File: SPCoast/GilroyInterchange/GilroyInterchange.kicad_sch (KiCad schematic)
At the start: 31 parts, among them SW777 777, SW781 781

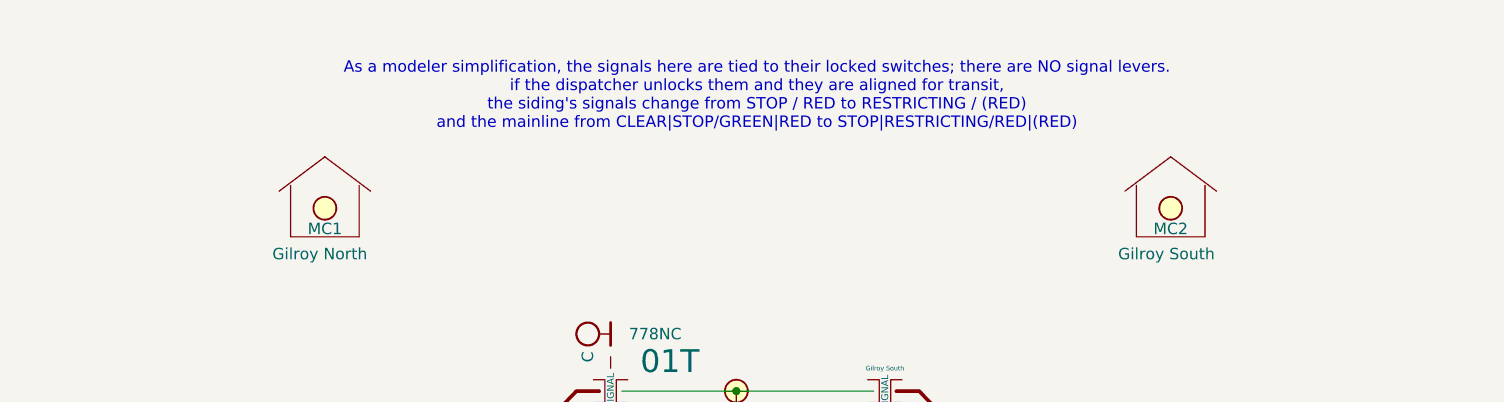
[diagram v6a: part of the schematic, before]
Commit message: SPCoast: owner's edits: Interlocking symbol on every Trackplan; MAIN HOUSE is STRUCTURE/CONTROL_POINT (baseline)
Each plant has one Interlocking symbol (Value is the authoritative name) and
every MAIN HOUSE's Interlocking pin is wired to it. Library Role/Kind:
Interlocking is STRUCTURE/INTERLOCKING, MAIN HOUSE is STRUCTURE/CONTROL_POINT
(refreshed on all instances by the owner).

Verified: one Interlocking symbol per plant; every house shares a net with it;
net counts are one higher than before in each plant (Christopher 34, Corporal
27, GilroyCalTrain 28, GilroyInterchange 23, Luchessa 35, Sargent 19,
Watsonville 97); no root-UUID regression; no symbol moved or removed.

Co-Authored-By: Claude Sonnet 5.5 <noreply@anthropic.com>
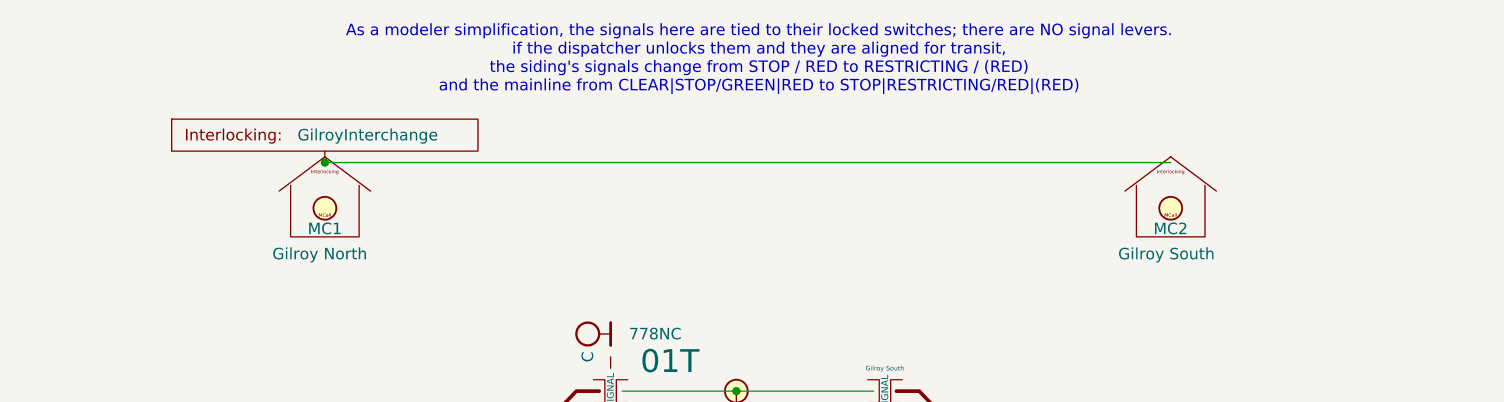
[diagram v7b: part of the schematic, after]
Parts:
- added Plant1: ${TITLE}, symbol Railroad:Interlocking
- HOUSE1, HOUSE2: Kind (none) -> CONTROL_POINT; Role CONTROL_POINT -> STRUCTURE
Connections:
- new net: HOUSE1.2 (Interlocking), HOUSE2.2 (Interlocking), Plant1.1 (Interlocking)
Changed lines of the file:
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@@
 	(text "As a modeler simplification, the signals here are tied to their locked switches; there are NO signal levers.\nif the dispatcher unlocks them and they are aligned for transit, \nthe siding's signals change from STOP / RED to RESTRICTING / (RED)\nand the mainline from CLEAR|STOP/GREEN|RED to STOP|RESTRICTING/RED|(RED)"
 		(exclude_from_sim no)
-		(at 122.936 28.194 0)
+		(at 123.19 24.13 0)
 		(effects
 			(font
@@
 	)
 	(junction
+		(at 74.93 35.56)
+		(diameter 0)
+		(color 0 0 0 0)
+	)
+	(junction
 		(at 63.5 77.47)
 		(diameter 0)
@@
 		(stroke
 			(width 0.4064)
+			(type default)
+		)
+	)
+	(wire
+		(pts
+			(xy 74.93 35.56) (xy 168.91 35.56)
+		)
+		(stroke
+			(width 0)
 			(type default)
 		)
@@
 			)
 		)
-		(property "Description" "Rrepresents the Control Point Maintainer Bungalow (plus optional Maintainer Call)"
+		(property "Description" "The Control Point Maintainer Bungalow (plus optional Maintainer Call)"
 			(at 168.91 46.355 0)
 			(hide yes)
@@
 		)
 		(property "Milepost" "78.1"
-			(at 168.91 46.36 0)
-			(hide yes)
-			(show_name no)
-			(do_not_autoplace no)
-			(effects
-				(font
-					(size 1.27 1.27)
-				)
-			)
-		)
-		(property "Role" "CONTROL_POINT"
-			(at 168.91 40.64 0)
+			(at 168.91 46.355 0)
+			(hide yes)
+			(show_name no)
+			(do_not_autoplace no)
+			(effects
+				(font
+					(size 1.27 1.27)
+				)
+			)
+		)
+		(property "Role" "STRUCTURE"
+			(at 153.67 38.1 0)
+			(hide yes)
+			(show_name no)
+			(do_not_autoplace no)
+			(effects
+				(font
+					(size 1.27 1.27)
+				)
+			)
+		)
+		(property "Kind" "CONTROL_POINT"
+			(at 155.575 40.132 0)
 			(hide yes)
 			(show_name no)
@@
 		)
 		(pin "1"
+		)
+		(pin "2"
 		)
 		(instances
@@
 	)
 	(symbol
+		(lib_id "Railroad:Interlocking")
+		(at 74.93 35.56 0)
+		(unit 1)
+		(body_style 1)
+		(exclude_from_sim no)
+		(in_bom yes)
+		(on_board yes)
+		(in_pos_files yes)
+		(dnp no)
+		(fields_autoplaced yes)
+		(property "Reference" "Plant1"
+			(at 60.706 29.718 0)
+			(hide yes)
+			(show_name no)
+			(do_not_autoplace no)
+			(effects
+				(font
+					(size 1.27 1.27)
+				)
+			)
+		)
+		(property "Value" "${TITLE}"
+			(at 71.882 32.512 0)
+			(show_name no)
+			(do_not_autoplace yes)
+			(effects
+				(font
+					(size 1.27 1.27)
+				)
+				(justify left)
+			)
+		)
+		(property "Footprint" ""
+			(at 74.93 35.56 0)
+			(hide yes)
+			(show_name no)
+			(do_not_autoplace no)
+			(effects
+				(font
+					(size 1.27 1.27)
+				)
+			)
+		)
+		(property "Datasheet" ""
+			(at 74.93 35.56 0)
+			(hide yes)
+			(show_name no)
+			(do_not_autoplace no)
+			(effects
+				(font
+					(size 1.27 1.27)
+				)
+			)
+		)
+		(property "Description" ""
+			(at 74.93 35.56 0)
+			(hide yes)
+			(show_name no)
+			(do_not_autoplace no)
+			(effects
+				(font
+					(size 1.27 1.27)
+				)
+			)
+		)
+		(property "Role" "STRUCTURE"
+			(at 63.627 25.908 0)
+			(hide yes)
+			(show_name no)
+			(do_not_autoplace no)
+			(effects
+				(font
+					(size 1.27 1.27)
+				)
+			)
+		)
+		(property "Kind" "INTERLOCKING"
+			(at 65.024 27.559 0)
+			(hide yes)
+			(show_name no)
+			(do_not_autoplace no)
+			(effects
+				(font
+					(size 1.27 1.27)
+				)
+			)
+		)
+		(pin "1"
+		)
+		(instances
+			(project "GilroyInterchange"
+				(path "/c4fcbe05-44d0-4e90-8003-c2ec16e00151"
+					(reference "Plant1")
+					(unit 1)
+				)
+			)
+		)
+	)
+	(symbol
 		(lib_id "Railroad:Track Circuit")
 		(at 182.88 77.47 0)
@@
 			)
 		)
-		(property "Description" "Rrepresents the Control Point Maintainer Bungalow (plus optional Maintainer Call)"
+		(property "Description" "The Control Point Maintainer Bungalow (plus optional Maintainer Call)"
 			(at 74.93 46.355 0)
 			(hide yes)
@@
 		)
 		(property "Milepost" "77.7"
-			(at 74.93 46.36 0)
-			(hide yes)
-			(show_name no)
-			(do_not_autoplace no)
-			(effects
-				(font
-					(size 1.27 1.27)
-				)
-			)
-		)
-		(property "Role" "CONTROL_POINT"
-			(at 74.93 40.64 0)
+			(at 74.93 46.355 0)
+			(hide yes)
+			(show_name no)
+			(do_not_autoplace no)
+			(effects
+				(font
+					(size 1.27 1.27)
+				)
+			)
+		)
+		(property "Role" "STRUCTURE"
+			(at 59.69 38.1 0)
+			(hide yes)
+			(show_name no)
+			(do_not_autoplace no)
+			(effects
+				(font
+					(size 1.27 1.27)
+				)
+			)
+		)
+		(property "Kind" "CONTROL_POINT"
+			(at 61.595 40.132 0)
 			(hide yes)
 			(show_name no)
@@
 		(pin "1"
 		)
+		(pin "2"
+		)
 		(instances

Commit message: SPCoast: owner's edits: Gilroy names normalized to the spaced form (baseline)
GilroyInterchange title block and the desk GilroyCalTrain column Interlocking values now use the spaced spelling; names without spaces normalize to the same value.

Verified: netlists rebuild; no UUID regression.

Co-Authored-By: Claude Sonnet 5.5 <noreply@anthropic.com>
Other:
- title: GilroyInterchange -> Gilroy Interchange
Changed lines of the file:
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@@
 	(paper "USLetter")
 	(title_block
-		(title "GilroyInterchange")
+		(title "Gilroy Interchange")
 		(date "2026.09")
 		(rev "1.0")
